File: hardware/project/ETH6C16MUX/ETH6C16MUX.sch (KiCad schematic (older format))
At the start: 0 parts

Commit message: USB update
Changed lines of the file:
@@
 encoding utf-8
 Sheet 1 8
-Title ""
+Title "Main"
 Date ""
 Rev ""
@@
 F0 "MCU" 50
 F1 "MCU.sch" 50
+F2 "MCU_TX_UART3" O R 7350 2800 50
+F3 "MCU_RX_UART3" I R 7350 2900 50
+F4 "ETH_RMII_REF_CLK" I R 7350 4450 50
+F5 "ETH_~INT" B R 7350 4350 50
+F6 "ETH_~RST" B R 7350 4250 50
+F7 "ETH_RMII_MDC" B R 7350 4150 50
+F8 "ETH_RMII_MDIO" B R 7350 4050 50
+F9 "ETH_RMII_CRS_DV" B R 7350 3950 50
+F10 "ETH_RMII_RX1" B R 7350 3850 50
+F11 "ETH_RMII_RX0" B R 7350 3750 50
+F12 "ETH_RMII_TXEN" B R 7350 3650 50
+F13 "ETH_RMII_TX0" B R 7350 3550 50
+F14 "ETH_RMII_TX1" B R 7350 3450 50
 $EndSheet
 $Sheet
@@
 $EndSheet
 $Sheet
-S 7650 2550 1200 500
+S 7650 2700 1200 350
 U 5D737AE2
 F0 "USB" 50
 F1 "USB.sch" 50
-F2 "USB_D+" B L 7650 2650 50
-F3 "USB_D-" B L 7650 2750 50
-F4 "USB_ID" O L 7650 2850 50
-F5 "USB_VBUS" O L 7650 2950 50
+F2 "MCU_TX_UART3" I L 7650 2800 50
+F3 "MCU_RX_UART3" O L 7650 2900 50
 $EndSheet
 $Sheet
@@
 Wire Wire Line
 	2750 1450 9150 1450
+Wire Wire Line
+	7350 4450 7650 4450
+Wire Wire Line
+	7650 4350 7350 4350
+Wire Wire Line
+	7350 4250 7650 4250
+Wire Wire Line
+	7650 4150 7350 4150
+Wire Wire Line
+	7350 4050 7650 4050
+Wire Wire Line
+	7650 3950 7350 3950
+Wire Wire Line
+	7350 3850 7650 3850
+Wire Wire Line
+	7350 3750 7650 3750
+Wire Wire Line
+	7650 3650 7350 3650
+Wire Wire Line
+	7350 3550 7650 3550
+Wire Wire Line
+	7650 3450 7350 3450
+Wire Wire Line
+	7350 2900 7650 2900
+Wire Wire Line
+	7650 2800 7350 2800
+Wire Wire Line
+	8850 3450 9150 3450
+Wire Wire Line
+	9150 3550 8850 3550
+Wire Wire Line
+	8850 3750 9150 3750
+Wire Wire Line
+	9150 3850 8850 3850
 $EndSCHEMATC

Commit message: FPGA schematic
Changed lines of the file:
@@
 F13 "ETH_RMII_TX0" B R 7350 3550 50
 F14 "ETH_RMII_TX1" B R 7350 3450 50
+F15 "FPGA_SPI3_CS" O L 5450 2550 50
+F16 "FPGA_CFG_CS" O L 5450 2450 50
+F17 "MCU_SPI3_SCLK" O L 5450 1750 50
+F18 "MCU_SPI3_MISO" I L 5450 1850 50
+F19 "MCU_SPI3_MOSI" O L 5450 1950 50
+F20 "FPGA_CRESET_B" O L 5450 2050 50
+F21 "FPGA_CDONE" I L 5450 2150 50
+F22 "FPGA_CBSEL0" O L 5450 2250 50
+F23 "FPGA_CBSEL1" O L 5450 2350 50
 $EndSheet
 $Sheet

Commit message: Schematic design
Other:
- note added: "22u - C1210C226K3PAC7210\n470u - T523H477M016APE070\n2u2 - 08053C225K4Z2A\n1u - 06033C105KAT2A"
- note removed: "22u - EMJ325KB7226KMHP\n470u - T523H477M016APE070"

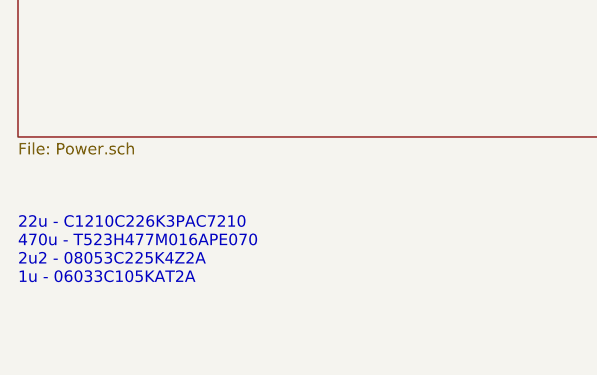
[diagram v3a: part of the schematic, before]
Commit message: PCB design, need to redesign of the board to board connectors.
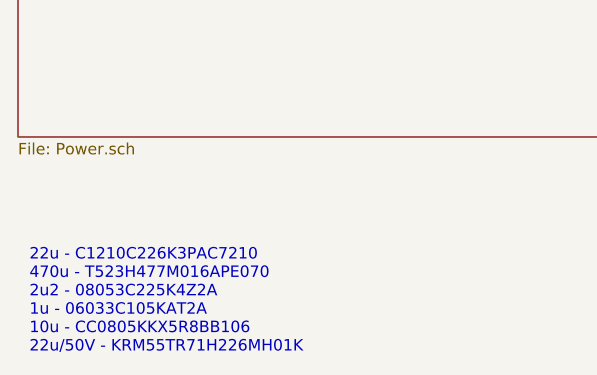
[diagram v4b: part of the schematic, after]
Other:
- note added: "22u - C1210C226K3PAC7210\n470u - T523H477M016APE070\n2u2 - 08053C225K4Z2A\n1u - 06033C105KAT2A\n10u - CC0805KKX5R8BB106\n22u/50V - KRM55TR71H226MH01K"
- note removed: "22u - C1210C226K3PAC7210\n470u - T523H477M016APE070\n2u2 - 08053C225K4Z2A\n1u - 06033C105KAT2A"
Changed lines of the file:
@@
 F8 "RELAY[0..53]" B R 2800 1750 50
 $EndSheet
-Text Notes 900  7000 0    50   ~ 0
-22u - C1210C226K3PAC7210\n470u - T523H477M016APE070\n2u2 - 08053C225K4Z2A\n1u - 06033C105KAT2A
+Text Notes 950  7300 0    50   ~ 0
+22u - C1210C226K3PAC7210\n470u - T523H477M016APE070\n2u2 - 08053C225K4Z2A\n1u - 06033C105KAT2A\n10u - CC0805KKX5R8BB106\n22u/50V - KRM55TR71H226MH01K
 $Sheet
 S 900  5450 7950 900

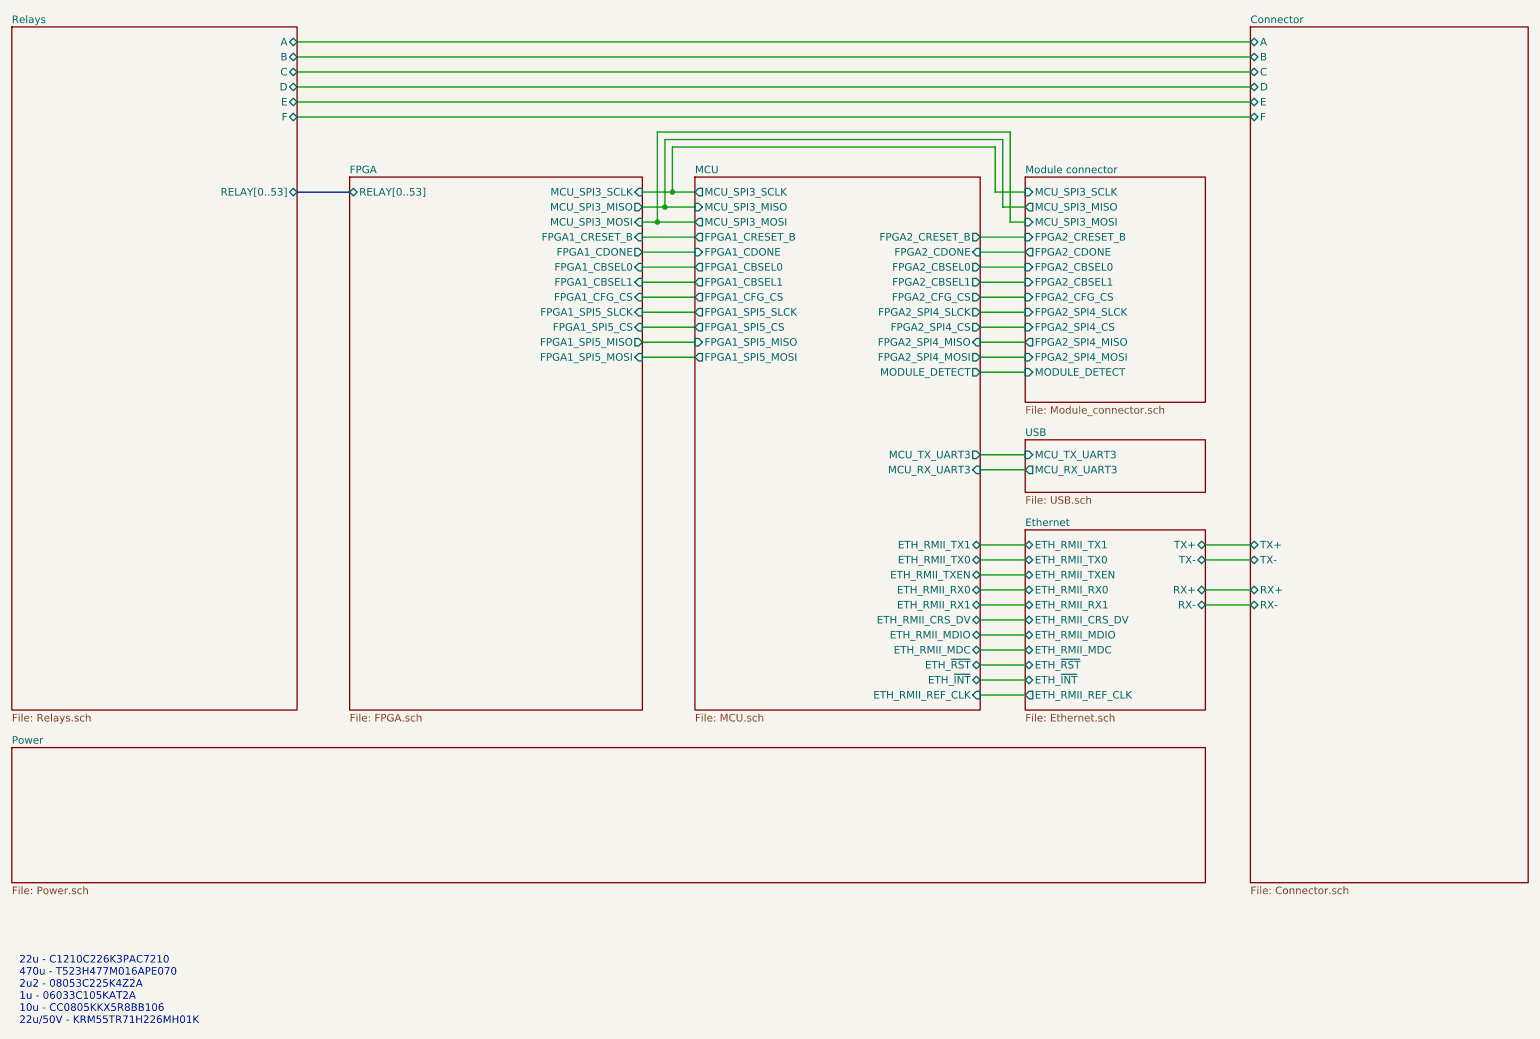
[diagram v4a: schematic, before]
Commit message: PCB layout, board to board connector changed.
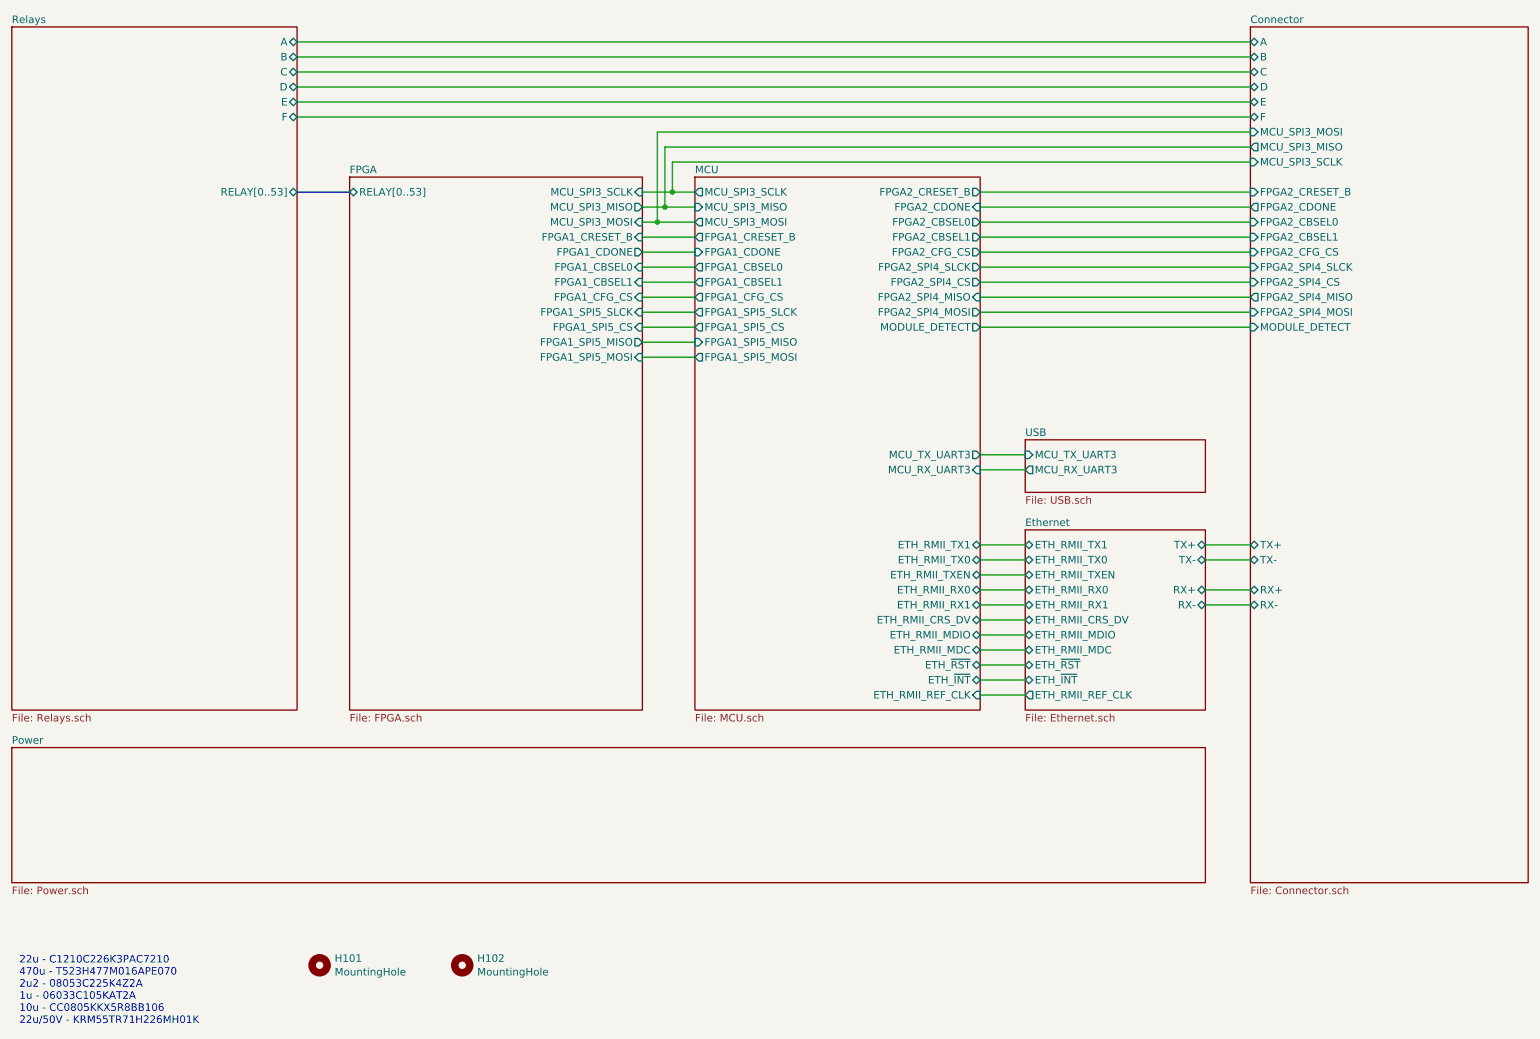
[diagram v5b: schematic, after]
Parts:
- added H101, H102: MountingHole, MountingHole:MountingHole_3.2mm_M3_DIN965_Pad, symbol Mechanical:MountingHole
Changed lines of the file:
@@
 $Descr A4 11693 8268
 encoding utf-8
-Sheet 1 9
+Sheet 1 8
 Title "Main"
 Date ""
@@
 F21 "FPGA1_CBSEL1" O L 5450 2350 50
 F22 "FPGA1_CFG_CS" O L 5450 2450 50
-F23 "FPGA2_CBSEL0" O R 7350 2250 50
-F24 "FPGA2_CBSEL1" O R 7350 2350 50
-F25 "FPGA2_CRESET_B" O R 7350 2050 50
-F26 "FPGA2_CDONE" I R 7350 2150 50
-F27 "FPGA2_CFG_CS" O R 7350 2450 50
-F28 "FPGA2_SPI4_SLCK" O R 7350 2550 50
-F29 "FPGA2_SPI4_CS" O R 7350 2650 50
-F30 "FPGA2_SPI4_MISO" I R 7350 2750 50
-F31 "FPGA2_SPI4_MOSI" O R 7350 2850 50
+F23 "FPGA2_CBSEL0" O R 7350 1950 50
+F24 "FPGA2_CBSEL1" O R 7350 2050 50
+F25 "FPGA2_CRESET_B" O R 7350 1750 50
+F26 "FPGA2_CDONE" I R 7350 1850 50
+F27 "FPGA2_CFG_CS" O R 7350 2150 50
+F28 "FPGA2_SPI4_SLCK" O R 7350 2250 50
+F29 "FPGA2_SPI4_CS" O R 7350 2350 50
+F30 "FPGA2_SPI4_MISO" I R 7350 2450 50
+F31 "FPGA2_SPI4_MOSI" O R 7350 2550 50
 F32 "FPGA1_SPI5_SLCK" O L 5450 2550 50
 F33 "FPGA1_SPI5_CS" O L 5450 2650 50
 F34 "FPGA1_SPI5_MISO" I L 5450 2750 50
 F35 "FPGA1_SPI5_MOSI" O L 5450 2850 50
-F36 "MODULE_DETECT" O R 7350 2950 50
+F36 "MODULE_DETECT" O R 7350 2650 50
 $EndSheet
 $Sheet
@@
 F10 "E" B L 9150 1150 50
 F11 "F" B L 9150 1250 50
+F12 "FPGA2_CFG_CS" I L 9150 2150 50
+F13 "FPGA2_SPI4_MOSI" I L 9150 2550 50
+F14 "FPGA2_SPI4_MISO" O L 9150 2450 50
+F15 "FPGA2_SPI4_CS" I L 9150 2350 50
+F16 "FPGA2_SPI4_SLCK" I L 9150 2250 50
+F17 "FPGA2_CDONE" O L 9150 1850 50
+F18 "FPGA2_CRESET_B" I L 9150 1750 50
+F19 "FPGA2_CBSEL1" I L 9150 2050 50
+F20 "FPGA2_CBSEL0" I L 9150 1950 50
+F21 "MCU_SPI3_MOSI" I L 9150 1350 50
+F22 "MCU_SPI3_MISO" O L 9150 1450 50
+F23 "MCU_SPI3_SCLK" I L 9150 1550 50
+F24 "MODULE_DETECT" I L 9150 2650 50
 $EndSheet
 Wire Wire Line
@@
 Wire Wire Line
 	5450 1750 5300 1750
-$Sheet
-S 7650 1650 1200 1500
-U 5D8B050C
-F0 "Module connector" 50
-F1 "Module_connector.sch" 50
-F2 "MCU_SPI3_SCLK" I L 7650 1750 50
-F3 "MCU_SPI3_MISO" O L 7650 1850 50
-F4 "MCU_SPI3_MOSI" I L 7650 1950 50
-F5 "FPGA2_CBSEL0" I L 7650 2250 50
-F6 "FPGA2_CBSEL1" I L 7650 2350 50
-F7 "FPGA2_CRESET_B" I L 7650 2050 50
-F8 "FPGA2_CDONE" O L 7650 2150 50
-F9 "FPGA2_SPI4_SLCK" I L 7650 2550 50
-F10 "FPGA2_SPI4_CS" I L 7650 2650 50
-F11 "FPGA2_SPI4_MISO" O L 7650 2750 50
-F12 "FPGA2_SPI4_MOSI" I L 7650 2850 50
-F13 "FPGA2_CFG_CS" I L 7650 2450 50
-F14 "MODULE_DETECT" I L 7650 2950 50
-$EndSheet
-Wire Wire Line
-	7450 1750 7650 1750
 Connection ~ 5300 1750
 Wire Wire Line
 	5300 1750 5100 1750
 Wire Wire Line
-	7500 1850 7650 1850
-Wire Wire Line
-	7650 1950 7550 1950
-Wire Wire Line
-	7450 1450 7450 1750
-Wire Wire Line
-	5300 1750 5300 1450
-Wire Wire Line
-	5300 1450 7450 1450
-Wire Wire Line
-	7500 1400 7500 1850
-Wire Wire Line
-	7550 1350 7550 1950
-Wire Wire Line
-	5250 1400 7500 1400
+	5300 1750 5300 1550
 Wire Wire Line
 	5250 1850 5450 1850
@@
 	5100 1850 5250 1850
 Wire Wire Line
-	5250 1850 5250 1400
-Wire Wire Line
-	5200 1350 7550 1350
+	5250 1850 5250 1450
 Wire Wire Line
 	5200 1950 5100 1950
@@
 Wire Wire Line
 	5200 1950 5200 1350
-Wire Wire Line
-	7350 2050 7650 2050
-Wire Wire Line
-	7350 2150 7650 2150
-Wire Wire Line
-	7350 2250 7650 2250
-Wire Wire Line
-	7350 2350 7650 2350
-Wire Wire Line
-	7350 2450 7650 2450
-Wire Wire Line
-	7350 2550 7650 2550
-Wire Wire Line
-	7650 2650 7350 2650
-Wire Wire Line
-	7350 2750 7650 2750
-Wire Wire Line
-	7350 2850 7650 2850
-Wire Wire Line
-	7350 2950 7650 2950
 Wire Bus Line
 	3150 1750 2800 1750
@@
 Wire Wire Line
 	9150 1250 2800 1250
+$Comp
+L Mechanical:MountingHole H101
+U 1 1 5D812530
+P 2950 6900
+F 0 "H101" H 3050 6946 50  0000 L CNN
+F 1 "MountingHole" H 3050 6855 50  0000 L CNN
+F 2 "MountingHole:MountingHole_3.2mm_M3_DIN965_Pad" H 2950 6900 50  0001 C CNN
+F 3 "~" H 2950 6900 50  0001 C CNN
+	1    2950 6900
+	1    0    0    -1
+$EndComp
+$Comp
+L Mechanical:MountingHole H102
+U 1 1 5D8126FD
+P 3900 6900
+F 0 "H102" H 4000 6946 50  0000 L CNN
+F 1 "MountingHole" H 4000 6855 50  0000 L CNN
+F 2 "MountingHole:MountingHole_3.2mm_M3_DIN965_Pad" H 3900 6900 50  0001 C CNN
+F 3 "~" H 3900 6900 50  0001 C CNN
+	1    3900 6900
+	1    0    0    -1
+$EndComp
+Wire Wire Line
+	7350 2650 9150 2650
+Wire Wire Line
+	9150 2550 7350 2550
+Wire Wire Line
+	7350 2450 9150 2450
+Wire Wire Line
+	9150 2350 7350 2350
+Wire Wire Line
+	9150 2250 7350 2250
+Wire Wire Line
+	7350 2150 9150 2150
+Wire Wire Line
+	9150 2050 7350 2050
+Wire Wire Line
+	7350 1950 9150 1950
+Wire Wire Line
+	9150 1850 7350 1850
+Wire Wire Line
+	7350 1750 9150 1750
+Wire Wire Line
+	5300 1550 9150 1550
+Wire Wire Line
+	5250 1450 9150 1450
+Wire Wire Line
+	5200 1350 9150 1350
 $EndSCHEMATC

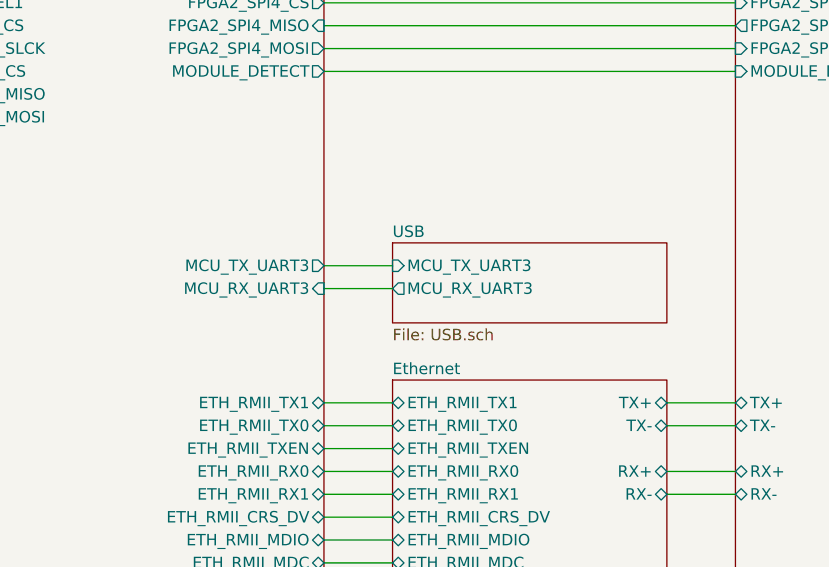
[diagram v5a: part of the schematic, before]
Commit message: PCB layout, deleted USB.
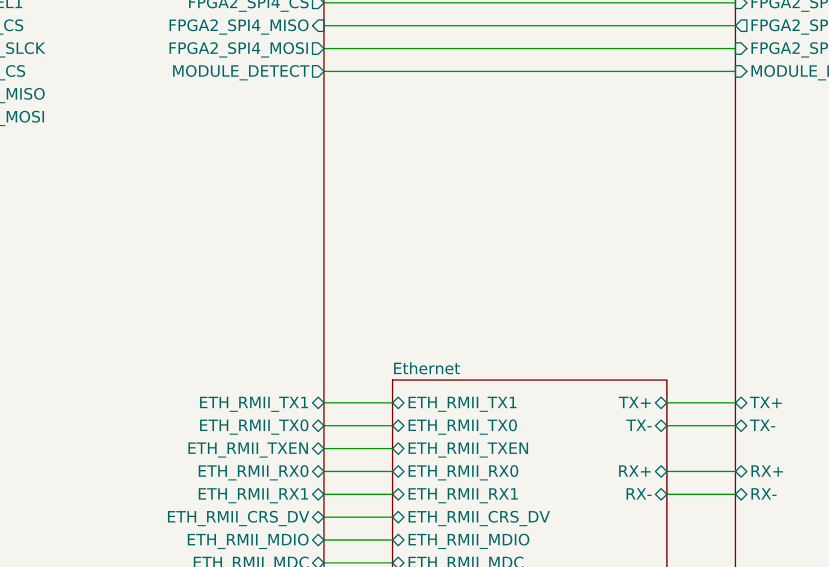
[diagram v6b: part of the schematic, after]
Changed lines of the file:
@@
 $Descr A4 11693 8268
 encoding utf-8
-Sheet 1 8
+Sheet 1 7
 Title "Main"
 Date ""
@@
 F0 "MCU" 50
 F1 "MCU.sch" 50
-F2 "MCU_TX_UART3" O R 7350 3500 50
-F3 "MCU_RX_UART3" I R 7350 3600 50
-F4 "ETH_RMII_REF_CLK" I R 7350 5100 50
-F5 "ETH_~INT" B R 7350 5000 50
-F6 "ETH_~RST" B R 7350 4900 50
-F7 "ETH_RMII_MDC" B R 7350 4800 50
-F8 "ETH_RMII_MDIO" B R 7350 4700 50
-F9 "ETH_RMII_CRS_DV" B R 7350 4600 50
-F10 "ETH_RMII_RX1" B R 7350 4500 50
-F11 "ETH_RMII_RX0" B R 7350 4400 50
-F12 "ETH_RMII_TXEN" B R 7350 4300 50
-F13 "ETH_RMII_TX0" B R 7350 4200 50
-F14 "ETH_RMII_TX1" B R 7350 4100 50
-F15 "MCU_SPI3_SCLK" O L 5450 1750 50
-F16 "MCU_SPI3_MISO" I L 5450 1850 50
-F17 "MCU_SPI3_MOSI" O L 5450 1950 50
-F18 "FPGA1_CRESET_B" O L 5450 2050 50
-F19 "FPGA1_CDONE" I L 5450 2150 50
-F20 "FPGA1_CBSEL0" O L 5450 2250 50
-F21 "FPGA1_CBSEL1" O L 5450 2350 50
-F22 "FPGA1_CFG_CS" O L 5450 2450 50
-F23 "FPGA2_CBSEL0" O R 7350 1950 50
-F24 "FPGA2_CBSEL1" O R 7350 2050 50
-F25 "FPGA2_CRESET_B" O R 7350 1750 50
-F26 "FPGA2_CDONE" I R 7350 1850 50
-F27 "FPGA2_CFG_CS" O R 7350 2150 50
-F28 "FPGA2_SPI4_SLCK" O R 7350 2250 50
-F29 "FPGA2_SPI4_CS" O R 7350 2350 50
-F30 "FPGA2_SPI4_MISO" I R 7350 2450 50
-F31 "FPGA2_SPI4_MOSI" O R 7350 2550 50
-F32 "FPGA1_SPI5_SLCK" O L 5450 2550 50
-F33 "FPGA1_SPI5_CS" O L 5450 2650 50
-F34 "FPGA1_SPI5_MISO" I L 5450 2750 50
-F35 "FPGA1_SPI5_MOSI" O L 5450 2850 50
-F36 "MODULE_DETECT" O R 7350 2650 50
+F2 "ETH_RMII_REF_CLK" I R 7350 5100 50
+F3 "ETH_~INT" B R 7350 5000 50
+F4 "ETH_~RST" B R 7350 4900 50
+F5 "ETH_RMII_MDC" B R 7350 4800 50
+F6 "ETH_RMII_MDIO" B R 7350 4700 50
+F7 "ETH_RMII_CRS_DV" B R 7350 4600 50
+F8 "ETH_RMII_RX1" B R 7350 4500 50
+F9 "ETH_RMII_RX0" B R 7350 4400 50
+F10 "ETH_RMII_TXEN" B R 7350 4300 50
+F11 "ETH_RMII_TX0" B R 7350 4200 50
+F12 "ETH_RMII_TX1" B R 7350 4100 50
+F13 "MCU_SPI3_SCLK" O L 5450 1750 50
+F14 "MCU_SPI3_MISO" I L 5450 1850 50
+F15 "MCU_SPI3_MOSI" O L 5450 1950 50
+F16 "FPGA1_CRESET_B" O L 5450 2050 50
+F17 "FPGA1_CDONE" I L 5450 2150 50
+F18 "FPGA1_CBSEL0" O L 5450 2250 50
+F19 "FPGA1_CBSEL1" O L 5450 2350 50
+F20 "FPGA1_CFG_CS" O L 5450 2450 50
+F21 "FPGA2_CBSEL0" O R 7350 1950 50
+F22 "FPGA2_CBSEL1" O R 7350 2050 50
+F23 "FPGA2_CRESET_B" O R 7350 1750 50
+F24 "FPGA2_CDONE" I R 7350 1850 50
+F25 "FPGA2_CFG_CS" O R 7350 2150 50
+F26 "FPGA2_SPI4_SLCK" O R 7350 2250 50
+F27 "FPGA2_SPI4_CS" O R 7350 2350 50
+F28 "FPGA2_SPI4_MISO" I R 7350 2450 50
+F29 "FPGA2_SPI4_MOSI" O R 7350 2550 50
+F30 "FPGA1_SPI5_SLCK" O L 5450 2550 50
+F31 "FPGA1_SPI5_CS" O L 5450 2650 50
+F32 "FPGA1_SPI5_MISO" I L 5450 2750 50
+F33 "FPGA1_SPI5_MOSI" O L 5450 2850 50
+F34 "MODULE_DETECT" O R 7350 2650 50
 $EndSheet
 $Sheet
@@
 F13 "FPGA1_SPI5_MISO" O R 5100 2750 50
 F14 "FPGA1_SPI5_MOSI" I R 5100 2850 50
-$EndSheet
-$Sheet
-S 7650 3400 1200 350
-U 5D737AE2
-F0 "USB" 50
-F1 "USB.sch" 50
-F2 "MCU_TX_UART3" I L 7650 3500 50
-F3 "MCU_RX_UART3" O L 7650 3600 50
 $EndSheet
 $Sheet
@@
 	7650 4100 7350 4100
 Wire Wire Line
-	7350 3600 7650 3600
-Wire Wire Line
-	7650 3500 7350 3500
-Wire Wire Line
 	9150 4100 8850 4100
